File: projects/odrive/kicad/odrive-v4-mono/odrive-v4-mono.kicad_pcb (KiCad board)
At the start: 4 copper layers, 140 x 112 mm, 325 parts, among them J1 PC 16/2-ST, J10 ENC_M1_JST-GH, J11 ENC_SPI_JST-GH, J12 GPIO_2x4, J13 BRAKE_EXT, J2 M0 A/B/C, J4 FTSH-105-01-L-DV-K, J5 FAN 12V 150mA MAX, J6 USB4105-GF-A, J7 JST-GH-4 CAN, J8 JST-GH-4 CAN, J9 ENC_M0_JST-GH, Q1 NVMFS5C628NL | BSC027N10NS5, Q10 NVMFS5C628NL, Q11 NVMFS5C628NL, Q12 NVMFS5C628NL, Q13 NVMFS5C628NL, Q14 NVMFS5C628NL, Q15 NVMFS5C628NL, Q16 NVMFS5C628NL, Q17 NVMFS5C628NL, Q18 NVMFS5C628NL, Q19 NVMFS5C628NL, Q20 NVMFS5C628NL, Q21 NVMFS5C628NL, Q50 NVMFS5C628NL/BSC027N10NS5, Q51 NVMFS5C628NL/BSC027N10NS5, SW1 CAN_TERM, U10 TLV9062, U11 TMUX1204, U12 TLV7031, U13 TLV431, U14 74LVC1G04, U15 74LVC1G08, U16 TPD4E05U06, U2 STM32F405RGT6, U20 LM5164DDA, U21 LMR51430, U22 TLV75533PDBV, U23 TPS7A2033DBV, U25 74LVC1G06, U26 TLV7031DBV, U27 74LVC1G08, U28 TPS3840DL30, U3 DRV8353RS, U30 TPS2553DBV, U31 TPS2553DBV, U32 TPS2553DBV, U33 USBLC6-2SC6, U34 TCAN1042HGV, U35 SN74LVC2G17, U36 SN74LVC2G17, U37 SN74LVC2G17, U38 TPD4E05U06, U39 TPD4E05U06, U40 SN74LVC1G125, U41 TPD4E05U06, U42 TPD1E10B06, U50 UCC27517A, U51 INA181A2, U52 TLV7031, U53 74LVC1G74, U54 74LVC1G32, U55 74LVC1G08, Y1 8MHz

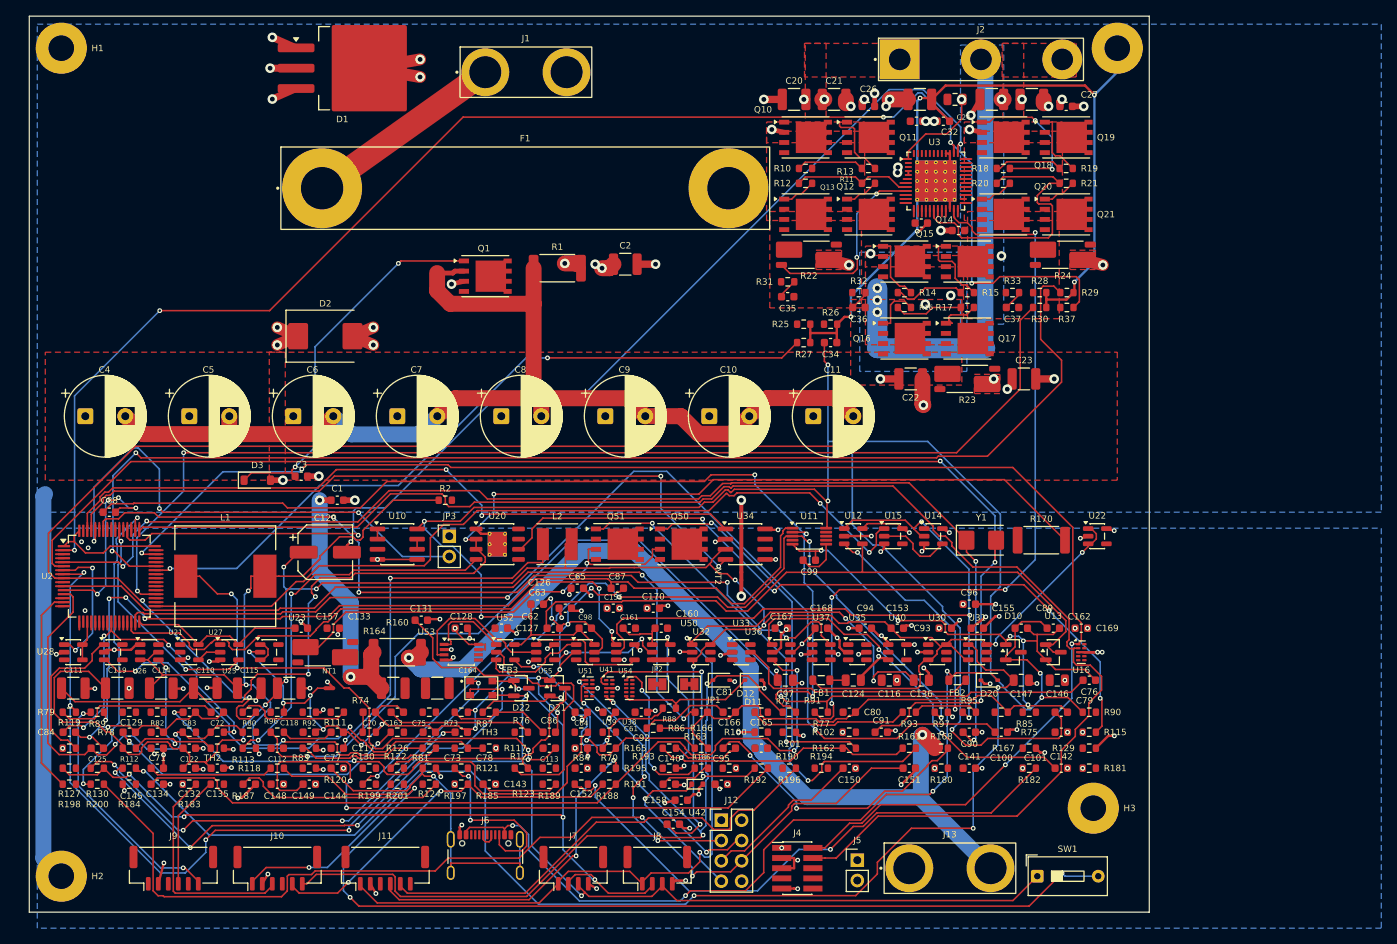
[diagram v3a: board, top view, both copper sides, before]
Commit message: Checkpoint ODrive 56 V recovery and modular handoff
Preserve corrected schematics, local libraries, partial PCB routing, firmware diagnostics, analysis tools and the independent modular-study handoff. The board remains incomplete with 381 unconnected items and 415 DRC warnings.

Validation: 52 host tests, ARM component compilation, schematic/PCB parity, native copper preservation, DRC, STEP export, Python lint, shellcheck and nix fmt. Known Konnect-generated schematic whitespace is retained. No fabrication or hardware validation is claimed.
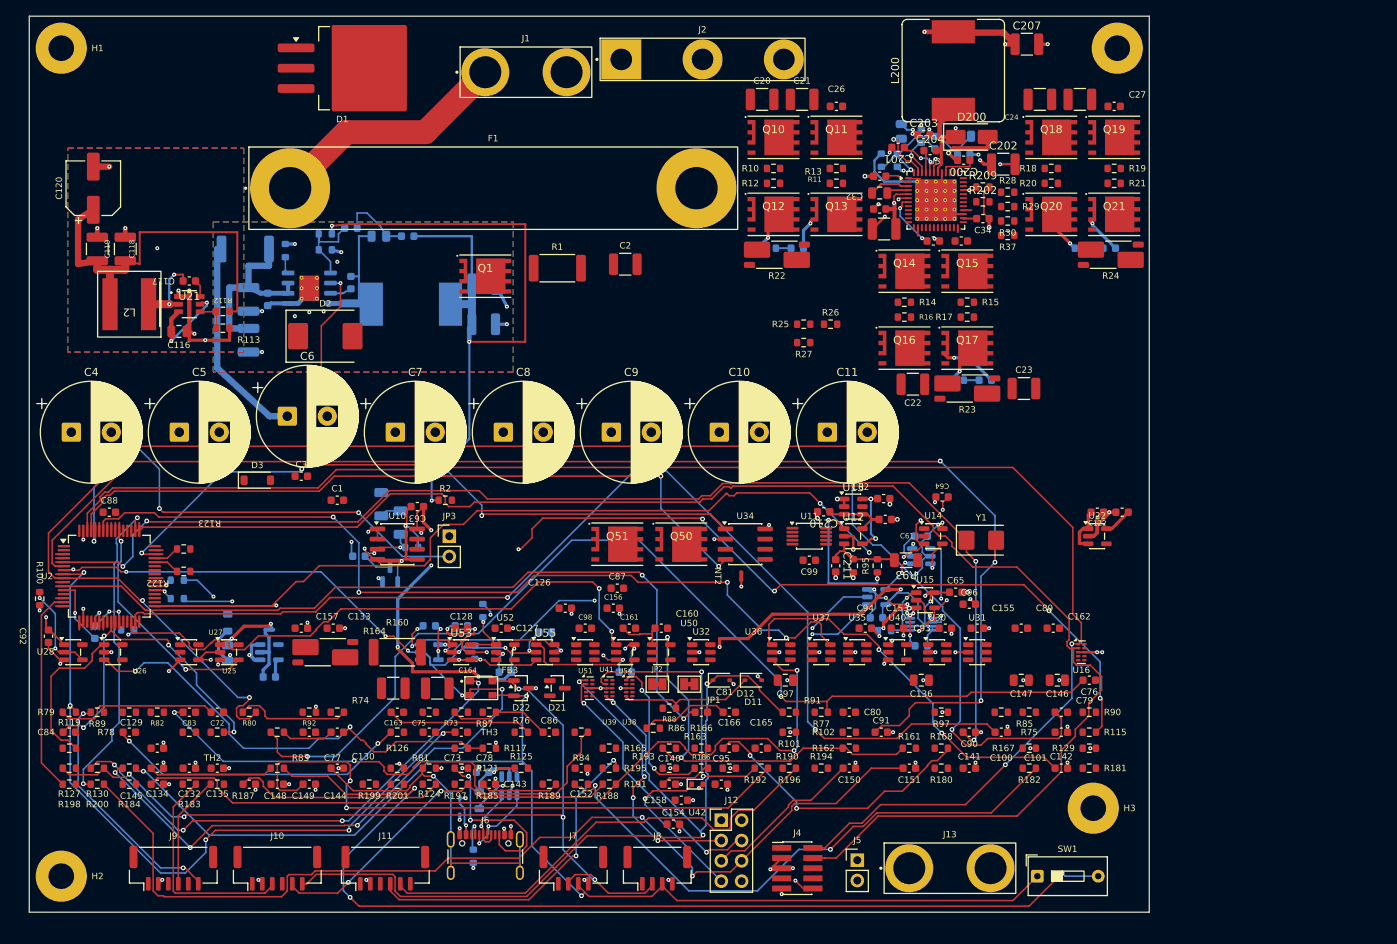
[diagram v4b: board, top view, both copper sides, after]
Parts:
- removed R96: 4.7k, Resistor_SMD:R_0603_1608Metric
- added C200: 1uF 25V X7R, Capacitor_SMD:C_0603_1608Metric, F.Cu at (166.8, 68.0)
- added C201: 470nF 25V X7R, Capacitor_SMD:C_0603_1608Metric, F.Cu at (158.6, 66.4)
- added C202: 2.2uF 100V X7R, Capacitor_SMD:C_1210_3225Metric, F.Cu at (171.8, 68.5)
- added C203: 100nF 100V X7R, Capacitor_SMD:C_0603_1608Metric, F.Cu at (161.8, 64.8)
- added C204: 10nF 50V X7R, Capacitor_SMD:C_0603_1608Metric, F.Cu at (162.6, 66.8)
- added C205: 3.3nF 100V C0G, Capacitor_SMD:C_0603_1608Metric, B.Cu at (166.8, 67.3)
- added C206: 100nF 50V X7R, Capacitor_SMD:C_0603_1608Metric, B.Cu at (163.2, 65.8)
- added C207: 22uF 50V X7R, Capacitor_SMD:C_1210_3225Metric, F.Cu at (174.7, 53.5)
- added C208: 100nF 16V X7R, Capacitor_SMD:C_0603_1608Metric, B.Cu at (161.5, 128.7)
- added C209: 100nF 16V X7R, Capacitor_SMD:C_0603_1608Metric, B.Cu at (161.5, 115.0)
- added C210: 1uF 16V X7R, Capacitor_SMD:C_0603_1608Metric, F.Cu at (149.3, 112.0)
- added C211: 100pF 50V C0G, Capacitor_SMD:C_0603_1608Metric, F.Cu at (150.8, 118.7)
- added C212: 100nF 16V X7R, Capacitor_SMD:C_0603_1608Metric, B.Cu at (100.0, 126.2)
- added C213: 100nF 16V X7R, Capacitor_SMD:C_0603_1608Metric, B.Cu at (155.9, 125.2)
- added C214: 10nF 100V C0G, Capacitor_SMD:C_0603_1608Metric, B.Cu at (97.3, 77.5)
- added C215: 330pF 50V C0G, Capacitor_SMD:C_0603_1608Metric, B.Cu at (90.2, 76.5)
- added D200: STPS1H100A, Diode_SMD:D_SMA, F.Cu at (167.8, 65.1)
- added L200: 330uH, Inductor_SMD:L_Bourns_SRR1260, F.Cu at (165.5, 56.8)
- added R202: 4.7k, Resistor_SMD:R_0603_1608Metric, F.Cu at (169.2, 73.2)
- added R203: 470k, Resistor_SMD:R_0805_2012Metric, B.Cu at (159.0, 64.4)
- added R204: 470k, Resistor_SMD:R_0603_1608Metric, B.Cu at (161.5, 65.0)
- added R205: 5.62k, Resistor_SMD:R_0603_1608Metric, B.Cu at (158.5, 68.0)
- added R206: 1k, Resistor_SMD:R_0603_1608Metric, B.Cu at (156.5, 68.0)
- added R207: 130k, Resistor_SMD:R_0805_2012Metric, B.Cu at (166.8, 65.0)
- added R208: 47k, Resistor_SMD:R_0603_1608Metric, B.Cu at (156.9, 126.8)
- added R209: 1k, Resistor_SMD:R_0603_1608Metric, F.Cu at (169.2, 71.3)
- added R210: 10k, Resistor_SMD:R_0603_1608Metric, B.Cu at (68.5, 122.8)
- added R211: 10.5k, Resistor_SMD:R_1206_3216Metric, B.Cu at (94.0, 111.0)
- added R212: 10k, Resistor_SMD:R_0603_1608Metric, B.Cu at (106.7, 124.3)
- added R213: 10k, Resistor_SMD:R_0603_1608Metric, B.Cu at (68.5, 120.5)
- added R214: 1k, Resistor_SMD:R_0603_1608Metric, B.Cu at (105.7, 129.5)
- added R215: 68.1k, Resistor_SMD:R_0805_2012Metric, B.Cu at (93.7, 77.5)
- added U56: 74LVC1G74, Package_SO:VSSOP-8_2.3x2mm_P0.5mm, B.Cu at (161.5, 126.0)
- added U57: 74LVC1G11, Package_TO_SOT_SMD:SOT-23-6, B.Cu at (161.5, 117.5)
- added U58: 74LVC1G14, Package_TO_SOT_SMD:SOT-23-5, B.Cu at (100.0, 129.5)
- added U59: 74LVC1G08, Package_TO_SOT_SMD:SOT-23-5, B.Cu at (155.9, 122.6)
- C10, C11, C4, C5, C6, C7, C8, C9: value 470uF/35V | 220uF/63V -> 220uF 100V; footprint Capacitor_THT:CP_Radial_D10.0mm_P5.00mm -> Capacitor_THT:CP_Radial_D12.5mm_P5.00mm
- C110, C111, C112, C114, C115, C124, C125, C131, C168, C169, C170, C35, C36, C37, C70, C71, D10, D20, FB1, FB2, NT1, R110, R111, R120, R170, R31, R32, R33, R71, R72, U20, U23, U33: moved to B.Cu
- C113: value 100nF 25V -> 2.2nF 50V X7R; moved to B.Cu
- C167: value 100nF -> 100nF 16V X7R; moved to B.Cu
- C30, C31: value 1uF -> 1uF 25V X7R
- C32: value 1uF 100V X7R -> 22uF 50V X7R
- C33: value 100nF -> 100nF 50V X7R
- C62: value 100nF -> 1uF 16V X7R
- D2: value SMDJ28A | SMDJ58A -> SMDJ58A
- L1: footprint Inductor_SMD:L_12x12mm_H8mm -> Inductor_SMD:L_Wuerth_WE-PD-Typ-LS; moved to B.Cu
- L2: value 4.7uH -> 6.8uH; footprint Inductor_SMD:L_Taiyo-Yuden_NR-50xx -> odrive-mono:Coilcraft_XAL7070_682
- Q1: value NVMFS5C628NL | BSC027N10NS5 -> BSC027N10NS5; footprint Package_SO:PowerPAK_SO-8_Single -> odrive-mono:Infineon_PG-TSON-8-3
- Q10, Q11, Q12, Q13, Q14, Q15, Q16, Q17, Q18, Q19, Q20, Q21: value NVMFS5C628NL -> BSC027N10NS5; footprint Package_SO:PowerPAK_SO-8_Single -> odrive-mono:Infineon_PG-TSON-8-3
- Q50, Q51: value NVMFS5C628NL/BSC027N10NS5 -> BSC027N10NS5; footprint Package_SO:PowerPAK_SO-8_Single -> odrive-mono:Infineon_PG-TSON-8-3
- R118: value 301k -> 75k; moved to B.Cu
- R70: value 10k | 18k -> 10.5k; footprint Resistor_SMD:R_0603_1608Metric -> Resistor_SMD:R_1206_3216Metric; moved to B.Cu
- R93: value 12k | 15.4k -> 455k; footprint Resistor_SMD:R_0603_1608Metric -> Resistor_SMD:R_1206_3216Metric
- R95: value 130k -> 301k
- U12, U52: value TLV7031 -> TLV3201AIDBVR
- U13: value TLV431 -> REF35125QDBVR; footprint Package_TO_SOT_SMD:SOT-23 -> Package_TO_SOT_SMD:SOT-23-6
- U21: value LMR51430 -> LMR51430XFDDCR; footprint Package_TO_SOT_SMD:SOT-23-6 -> odrive-mono:TI_DDC0006A
- U25: value 74LVC1G06 -> 74LVC1G07
- U53: value 74LVC1G74 -> 74LVC1G3208; footprint Package_SO:TSSOP-8_3x3mm_P0.65mm -> Package_TO_SOT_SMD:SOT-23-6
- U55: value 74LVC1G08 -> 74LVC1G11; footprint Package_TO_SOT_SMD:SOT-23-5 -> Package_TO_SOT_SMD:SOT-23-6
- moved C122 117.3 mm to (183.5, 112.0)
- moved R170 105.9 mm to (77.0, 79.1)
- moved C116 98.9 mm to (68.7, 89.4)
- moved R100 91.7 mm to (51.3, 122.8), turned to -90 degrees
- moved R72 79.9 mm to (62.3, 126.7), turned to 180 degrees
- moved D10 78.5 mm to (95.1, 119.8), turned to 90 degrees
- moved C124 78.3 mm to (74.8, 129.6), turned to 90 degrees
- moved C92 74.7 mm to (52.4, 127.5), turned to -90 degrees
- moved FB1 74.5 mm to (74.8, 125.8), turned to -90 degrees
- moved R94 74.3 mm to (153.0, 118.7), turned to -90 degrees
- moved C123 73.8 mm to (186.6, 112.0), turned to 180 degrees
- moved D20 68.1 mm to (103.8, 148.8), turned to 90 degrees
- moved R110 65.6 mm to (87.0, 77.2), turned to 180 degrees
- moved C114 64.6 mm to (106.8, 83.5)
- moved C113 63.3 mm to (90.2, 83.3), turned to 90 degrees
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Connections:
- net /Rails/PG_ALL renamed RAILS_OK
- C167 pad 1: VCC -> AVCC
- C167 pad 2: GND -> AGND
- C32 pad 1: DCBUS -> /MotorCell M0/M0_VM
- C33 pad 1: DCBUS -> /MotorCell M0/M0_VM
- C62 pad 2: AGND -> GND
- D2 pad 1: PGND -> DCBUS
- D2 pad 2: DCBUS -> PGND
- Q1 pad 1: /Power Input & Protection/Q1_GATE -> PGND
- Q1 pad 2: /Power Input & Protection/BULK_RTN -> PGND
- Q1 pad 4: (no net) -> /Power Input & Protection/Q1_GATE
- Q1 pad 5: (no net) -> /Power Input & Protection/BULK_RTN
- Q10 pad 1: /MotorCell M0/M0_GHA1 -> /MotorCell M0/M0_A
- Q10 pad 2: DCBUS -> /MotorCell M0/M0_A
- Q10 pad 4: (no net) -> /MotorCell M0/M0_GHA1
- Q10 pad 5: (no net) -> DCBUS
- Q11 pad 1: /MotorCell M0/M0_GHA2 -> /MotorCell M0/M0_A
- Q11 pad 2: DCBUS -> /MotorCell M0/M0_A
- Q11 pad 4: (no net) -> /MotorCell M0/M0_GHA2
- Q11 pad 5: (no net) -> DCBUS
- Q12 pad 1: /MotorCell M0/M0_GLA1 -> /MotorCell M0/M0_SRC_A
- Q12 pad 2: /MotorCell M0/M0_A -> /MotorCell M0/M0_SRC_A
- Q12 pad 4: (no net) -> /MotorCell M0/M0_GLA1
- Q12 pad 5: (no net) -> /MotorCell M0/M0_A
- Q13 pad 1: /MotorCell M0/M0_GLA2 -> /MotorCell M0/M0_SRC_A
- Q13 pad 2: /MotorCell M0/M0_A -> /MotorCell M0/M0_SRC_A
- Q13 pad 4: (no net) -> /MotorCell M0/M0_GLA2
- Q13 pad 5: (no net) -> /MotorCell M0/M0_A
- Q14 pad 1: /MotorCell M0/M0_GHB1 -> /MotorCell M0/M0_B
- Q14 pad 2: DCBUS -> /MotorCell M0/M0_B
- Q14 pad 4: (no net) -> /MotorCell M0/M0_GHB1
- Q14 pad 5: (no net) -> DCBUS
- Q15 pad 1: /MotorCell M0/M0_GHB2 -> /MotorCell M0/M0_B
- Q15 pad 2: DCBUS -> /MotorCell M0/M0_B
- Q15 pad 4: (no net) -> /MotorCell M0/M0_GHB2
- Q15 pad 5: (no net) -> DCBUS
- Q16 pad 1: /MotorCell M0/M0_GLB1 -> /MotorCell M0/M0_SRC_B
- Q16 pad 2: /MotorCell M0/M0_B -> /MotorCell M0/M0_SRC_B
- Q16 pad 4: (no net) -> /MotorCell M0/M0_GLB1
- Q16 pad 5: (no net) -> /MotorCell M0/M0_B
- Q17 pad 1: /MotorCell M0/M0_GLB2 -> /MotorCell M0/M0_SRC_B
- Q17 pad 2: /MotorCell M0/M0_B -> /MotorCell M0/M0_SRC_B
- Q17 pad 4: (no net) -> /MotorCell M0/M0_GLB2
- Q17 pad 5: (no net) -> /MotorCell M0/M0_B
- Q18 pad 1: /MotorCell M0/M0_GHC1 -> /MotorCell M0/M0_C
- Q18 pad 2: DCBUS -> /MotorCell M0/M0_C
- Q18 pad 4: (no net) -> /MotorCell M0/M0_GHC1
- Q18 pad 5: (no net) -> DCBUS
- Q19 pad 1: /MotorCell M0/M0_GHC2 -> /MotorCell M0/M0_C
- Q19 pad 2: DCBUS -> /MotorCell M0/M0_C
- Q19 pad 4: (no net) -> /MotorCell M0/M0_GHC2
- Q19 pad 5: (no net) -> DCBUS
- Q20 pad 1: /MotorCell M0/M0_GLC1 -> /MotorCell M0/M0_SRC_C
- Q20 pad 2: /MotorCell M0/M0_C -> /MotorCell M0/M0_SRC_C
- Q20 pad 4: (no net) -> /MotorCell M0/M0_GLC1
- Q20 pad 5: (no net) -> /MotorCell M0/M0_C
- Q21 pad 1: /MotorCell M0/M0_GLC2 -> /MotorCell M0/M0_SRC_C
- Q21 pad 2: /MotorCell M0/M0_C -> /MotorCell M0/M0_SRC_C
- Q21 pad 4: (no net) -> /MotorCell M0/M0_GLC2
- Q21 pad 5: (no net) -> /MotorCell M0/M0_C
- Q50 pad 1: /Brake Chopper/BRK_G0 -> /Brake Chopper/BRK_SRC
- Q50 pad 2: /Brake Chopper/BRK_SW -> /Brake Chopper/BRK_SRC
- Q50 pad 4: (no net) -> /Brake Chopper/BRK_G0
- Q50 pad 5: (no net) -> /Brake Chopper/BRK_SW
- Q51 pad 1: /Brake Chopper/BRK_G1 -> /Brake Chopper/BRK_SRC
- Q51 pad 2: /Brake Chopper/BRK_SW -> /Brake Chopper/BRK_SRC
- Q51 pad 4: (no net) -> /Brake Chopper/BRK_G1
- Q51 pad 5: (no net) -> /Brake Chopper/BRK_SW
- R70 pad 1: DCBUS -> /Sensing/VBUS_DIV_TOP
- R93 pad 1: /Sensing/VBUS_S_BUF -> DCBUS
- R94 pad 2: AGND -> GND
- U11 pad 1: /Sensing/M0_MOTOR_THERM_F -> MUX_A0
- U11 pad 10: AVCC -> GPIO_6
- U11 pad 2: /Sensing/M1_MOTOR_THERM_F -> /Sensing/M0_MOTOR_THERM_F
- U11 pad 3: GPIO_6 -> AGND
- U11 pad 4: MUX_A0 -> BRAKE_ISENSE
- U11 pad 5: AGND -> AVCC
- U11 pad 7: ADC_AUX -> USB_VBUS_SENSE
- U11 pad 8: USB_VBUS_SENSE -> ADC_AUX
- U11 pad 9: BRAKE_ISENSE -> /Sensing/M1_MOTOR_THERM_F
- U13 pad 1: VREF_OV -> GND
- U13 pad 2: AGND -> GND
- U13 pad 3: VREF_OV -> VCC
- U15 pad 2: /Sensing/OV_LATCH_N -> /Sensing/DRV_ARMED
- U2 pad 37: M1_AH -> DRV_ENABLE_FB
- U2 pad 38: M1_BH -> BRK_OK_FB
- U25 pad 1: (no net) -> unconnected-(U25-NC-Pad1)
- U28 pad 2: GND -> VCC
- U28 pad 3: unconnected-(U28-CT-Pad3) -> GND
- U28 pad 5: VCC -> unconnected-(U28-CT-Pad5)
- U3 pad 1: /MotorCell M0/M0_CPL -> GND
- U3 pad 10: /MotorCell M0/M0_SN_A -> /MotorCell M0/M0_GLA
- U3 pad 11: /MotorCell M0/M0_GHB -> /MotorCell M0/M0_SP_A
- U3 pad 12: /MotorCell M0/M0_B -> /MotorCell M0/M0_SN_A
- U3 pad 13: /MotorCell M0/M0_GLB -> /MotorCell M0/M0_SN_B
- U3 pad 15: /MotorCell M0/M0_SN_B -> /MotorCell M0/M0_GLB
- U3 pad 16: /MotorCell M0/M0_GHC -> /MotorCell M0/M0_B
- U3 pad 17: /MotorCell M0/M0_C -> /MotorCell M0/M0_GHB
- U3 pad 18: /MotorCell M0/M0_GLC -> /MotorCell M0/M0_GHC
- U3 pad 19: /MotorCell M0/M0_SP_C -> /MotorCell M0/M0_C
- U3 pad 2: /MotorCell M0/M0_CPH -> /MotorCell M0/M0_VGLS
- U3 pad 20: /MotorCell M0/M0_SN_C -> /MotorCell M0/M0_GLC
- U3 pad 21: /MotorCell M0/M0_VGLS -> /MotorCell M0/M0_SP_C
- U3 pad 22: GND -> /MotorCell M0/M0_SN_C
- U3 pad 23: M0_SO3 -> M0_SO2
- U3 pad 25: M0_SO2 -> M0_SO3
- U3 pad 27: DRV_ENABLE -> GND
- U3 pad 29: M0_AH -> SPI3_MISO
- U3 pad 3: /MotorCell M0/M0_VCP -> /MotorCell M0/M0_CPL
- U3 pad 30: M0_AL -> SPI3_MOSI
- U3 pad 31: M0_BH -> SPI3_SCK
- U3 pad 32: M0_BL -> M0_nCS
- U3 pad 33: M0_CH -> DRV_ENABLE
- U3 pad 34: M0_CL -> M0_AH
- U3 pad 35: SPI3_SCK -> M0_AL
- U3 pad 36: SPI3_MOSI -> M0_BH
- U3 pad 37: SPI3_MISO -> M0_BL
- U3 pad 38: M0_nCS -> M0_CH
- U3 pad 39: GND -> M0_CL
- U3 pad 4: DCBUS -> /MotorCell M0/M0_CPH
- U3 pad 40: GND -> /MotorCell M0/M0_DVDD
- U3 pad 41: unconnected-(U3-SW-Pad41) -> GND
- U3 pad 42: unconnected-(U3-CB-Pad42) -> /MotorCell M0/M0_BUCK_SW
- U3 pad 43: unconnected-(U3-FB-Pad43) -> DCBUS
- U3 pad 44: unconnected-(U3-NC-Pad44) -> /MotorCell M0/M0_BUCK_VCC
- U3 pad 45: unconnected-(U3-NC-Pad45) -> /MotorCell M0/M0_BUCK_BST
- U3 pad 46: unconnected-(U3-NC-Pad46) -> /MotorCell M0/M0_BUCK_RCL
- U3 pad 47: unconnected-(U3-NC-Pad47) -> /MotorCell M0/M0_BUCK_RT
- U3 pad 48: unconnected-(U3-NC-Pad48) -> /MotorCell M0/M0_BUCK_FB
- U3 pad 5: DCBUS -> /MotorCell M0/M0_VM
- U3 pad 6: /MotorCell M0/M0_GHA -> DCBUS
- U3 pad 7: /MotorCell M0/M0_A -> /MotorCell M0/M0_VCP
- U3 pad 8: /MotorCell M0/M0_GLA -> /MotorCell M0/M0_GHA
- U3 pad 9: /MotorCell M0/M0_SP_A -> /MotorCell M0/M0_A
- U30 pad 1: /Encoders & GPIO/ENC_5V_M0 -> +5V
- U30 pad 4: /Encoders & GPIO/M0_ILIM -> unconnected-(U30-~{FAULT}-Pad4)
- U30 pad 5: unconnected-(U30-~{FAULT}-Pad5) -> /Encoders & GPIO/M0_ILIM
- U30 pad 6: +5V -> /Encoders & GPIO/ENC_5V_M0
- U31 pad 1: /Encoders & GPIO/ENC_5V_M1 -> +5V
- U31 pad 4: /Encoders & GPIO/M1_ILIM -> unconnected-(U31-~{FAULT}-Pad4)
- U31 pad 5: unconnected-(U31-~{FAULT}-Pad5) -> /Encoders & GPIO/M1_ILIM
- U31 pad 6: +5V -> /Encoders & GPIO/ENC_5V_M1
- U32 pad 1: AUX_5V -> +5V
- U32 pad 4: Net-(U32-ILIM) -> unconnected-(U32-~{FAULT}-Pad4)
- U32 pad 5: unconnected-(U32-~{FAULT}-Pad5) -> Net-(U32-ILIM)
- U32 pad 6: +5V -> AUX_5V
- U50 pad 2: /Brake Chopper/BRK_GATE -> PGND
- U50 pad 3: PGND -> /Brake Chopper/BRK_GATE
- U52 pad 1: /Brake Chopper/BRK_TRIP -> /Brake Chopper/BRK_OC_N
- U52 pad 3: BRAKE_ISENSE -> /Brake Chopper/BRK_TH
- U52 pad 4: /Brake Chopper/BRK_TH -> BRAKE_ISENSE
- U53 pad 1: /Brake Chopper/BRK_TRIP -> /Brake Chopper/BRK_RESET_ACTIVE
- U53 pad 2: VCC -> GND
- U53 pad 3: /Brake Chopper/BRK_OK -> BRK_OK
- U53 pad 4: GND -> BRK_OK
- U53 pad 5: unconnected-(U53-Q-Pad5) -> VCC
- U53 pad 6: NRST -> /Brake Chopper/BRK_OC_N
- U55 pad 2: /Brake Chopper/BRK_OK -> GND
- U55 pad 3: GND -> BRK_OK
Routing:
- net AVCC: track 283.3 -> 56.7 mm, vias 10 -> 7
- net AGND: track 291.1 -> 83.6 mm, vias 29 -> 7
- net +5V: track 257.5 -> 55.2 mm, vias 11 -> 0
- net M0_nCS: track 188.9 -> 0.00 mm, vias 5 -> 0
- net GND: track 281.6 -> 465.4 mm, vias 111 -> 147
- net NRST: track 17.6 -> 198.2 mm, vias 2 -> 10
- net M0_CH: track 157.2 -> 0.00 mm, vias 2 -> 0
- net DRV_ENABLE: track 1.00 -> 154.5 mm, vias 0 -> 4
- net M0_CL: track 142.8 -> 0.00 mm, vias 2 -> 0
- net /Encoders & GPIO/ENC_5V_M1: track 142.1 -> 0.00 mm, vias 4 -> 0
- net /Power Input & Protection/BULK_RTN: track 139.4 -> 0.00 mm
- net SPI3_MISO: track 137.7 -> 0.00 mm, vias 2 -> 0
- net /Rails/VIN_12: track 157.0 -> 23.7 mm, vias 4 -> 0
- net /Sensing/M1_MOTOR_THERM_F: track 125.4 -> 0.00 mm, vias 3 -> 0
- net AUX_5V: track 116.4 -> 0.00 mm, vias 4 -> 0
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- added copper zone on F.Cu, net GND
- removed copper zone on F.Cu, net /MotorCell M0/M0_A
- removed copper zone on B.Cu, net /MotorCell M0/M0_B
- removed copper zone on F.Cu, net /MotorCell M0/M0_B
- removed copper zone on F.Cu, net /MotorCell M0/M0_C
- removed copper zone on F.Cu, net /MotorCell M0/M0_SRC_A
- removed copper zone on F.Cu, net /MotorCell M0/M0_SRC_B
- removed copper zone on F.Cu, net /MotorCell M0/M0_SRC_C
- removed copper zone on In2.Cu, net AGND
- removed copper zone on F.Cu, net DCBUS
- removed copper zone on In2.Cu, net DCBUS
- removed copper zone on B.Cu, net PGND
- removed copper zone on F.Cu, net PGND
- removed copper zone on In1.Cu, net PGND
- removed copper zone on In2.Cu, net VCC
